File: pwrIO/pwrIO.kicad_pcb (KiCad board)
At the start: 4 copper layers, 33.7 x 30.3 mm, 55 parts, among them IC3 TLV61225DC, J1 MOTOR1, J2 MOTOR2, J3 VCC_MOTOR, J4 MOTOR1, J5 MOTOR2, J6 MISC, J7 ENC1, J8 ENC2, U1 TB6612FNG, U2 TB6612FNG

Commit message: sch pcb
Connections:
- R1 pad 1: /MOTOR_1/STBY -> /NB_B2
- R10 pad 1: /NB_B2 -> /MOTOR_2/PWMB
- R11 pad 1: /NB_B3 -> /NB_B5
- R12 pad 1: /NB_B4 -> /NB_A5
- R13 pad 1: /NB_B5 -> /NB_B6
- R14 pad 1: /NB_B6 -> /MOTOR_2/BIN2
- R2 pad 1: /NB_A1 -> /MOTOR_1/PWMA
- R3 pad 1: /NB_A2 -> /NB_A4
- R4 pad 1: /NB_A3 -> /NB_A2
- R5 pad 1: /NB_A4 -> /NB_B1
- R6 pad 1: /NB_A5 -> /NB_A3
- R7 pad 1: /NB_A6 -> /NB_B3
- R8 pad 1: /MOTOR_2/STBY -> /NB_A6
- R9 pad 1: /NB_B1 -> /NB_B4
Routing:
- net /NB_A4: track 7.34 -> 22.4 mm
- net /NB_A5: track 8.73 -> 23.4 mm
- net /NB_B6: track 0.00 -> 13.9 mm
- net /NB_A3: track 5.92 -> 19.2 mm
- net /NB_B2: track 0.00 -> 12.3 mm
- net /NB_B5: track 4.69 -> 15.9 mm
- net /NB_A6: track 10.5 -> 20.8 mm
- net /MOTOR_1/STBY: track 7.36 -> 0.00 mm
- net /NB_B4: track 11.8 -> 18.5 mm
- net /MOTOR_2/STBY: track 6.65 -> 0.00 mm
- net /NB_B3: track 9.80 -> 14.9 mm
- net /NB_A2: track 11.6 -> 16.3 mm
- net /NB_B1: track 13.0 -> 10.2 mm
- net /NB_A1: track 13.4 -> 14.9 mm

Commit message: sch pcb
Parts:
- C11, C5: moved to F.Cu
- moved C11 31.8 mm to (102.5, 70.4), turned to -90 degrees
- moved G*** 12.6 mm to (115.6, 83.7)
- moved C5 12.6 mm to (83.3, 70.3), turned to -90 degrees
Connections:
- R10 pad 1: /MOTOR_2/PWMB -> /NB_A8
- R14 pad 1: /MOTOR_2/BIN2 -> /NB_A7
- R2 pad 1: /MOTOR_1/PWMA -> /NB_A1
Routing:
- net /NB_A8: track 0.00 -> 19.8 mm
- net /NB_A7: track 0.00 -> 18.3 mm
- net /NB_B8: track 0.00 -> 10.9 mm
- net /NB_B7: track 0.00 -> 9.42 mm
- net GND1: track 34.9 -> 38.1 mm, vias 6 -> 9
- net GND: track 6.73 -> 8.53 mm, vias 4 -> 6

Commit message: pcb
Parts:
- moved G*** 11.7 mm to (104.1, 85.8)
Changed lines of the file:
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@@
 	(footprint "Cologne:open_cologne"
 		(layer "F.Cu")
-		(at 115.633146 83.705736)
+		(at 104.143146 85.825736)
 		(property "Reference" "G***"
 			(at 0 0 0)

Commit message: pcb
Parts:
- moved G*** 0.57 mm to (104.7, 85.9)
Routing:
- net VCC_MOTOR: track 30.9 -> 48.8 mm
- net +2V5: track 3.04 -> 10.2 mm
- net GND1: track 38.1 -> 44.7 mm
- net +3V3: track 20.9 -> 25.8 mm
- net GND: track 8.53 -> 11.3 mm, vias 6 -> 10

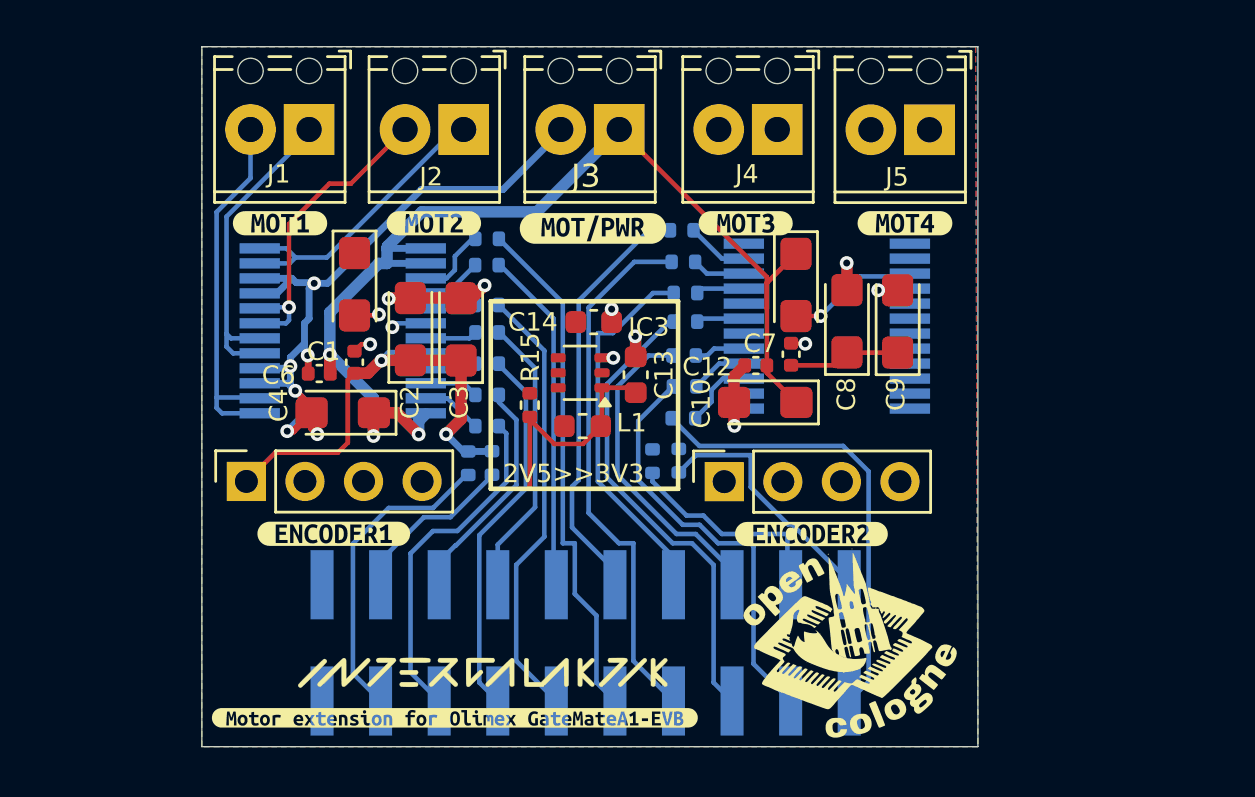
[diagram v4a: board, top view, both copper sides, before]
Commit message: Connecting encoder to 2.5V
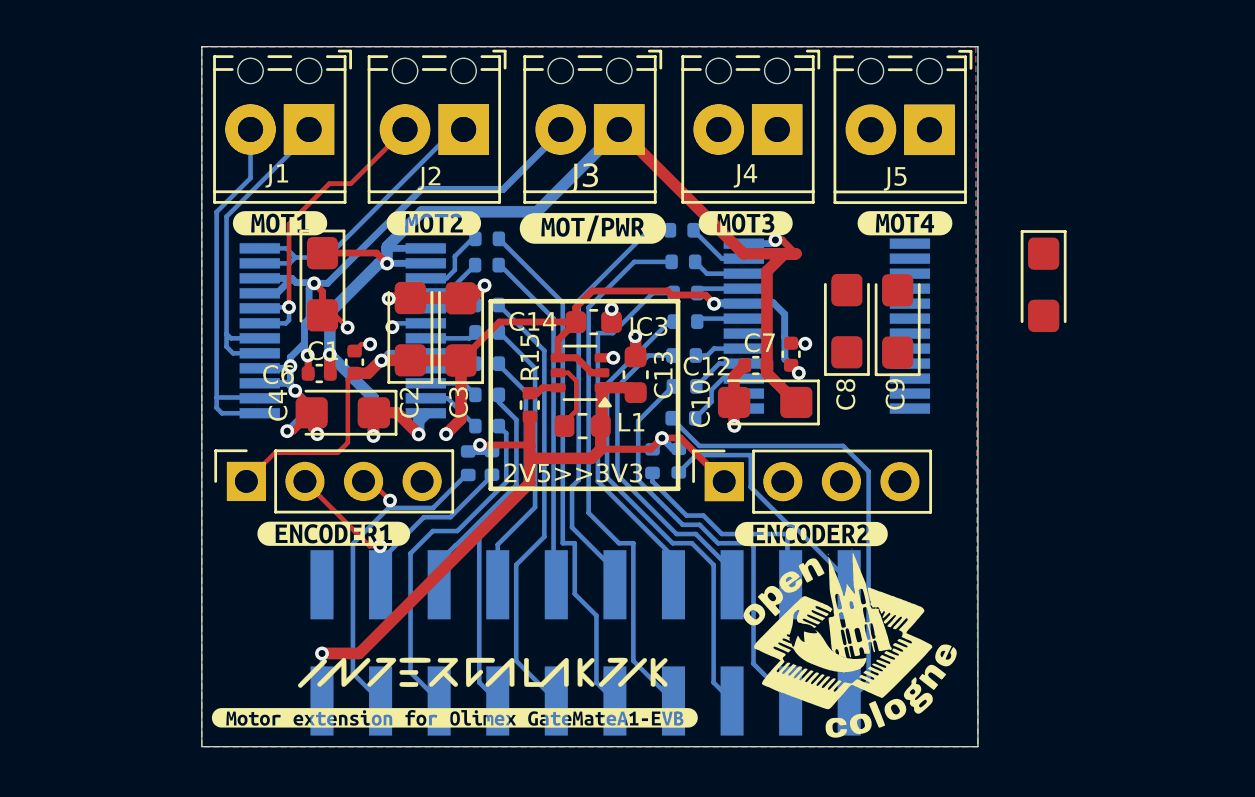
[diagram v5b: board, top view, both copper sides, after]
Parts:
- moved C11 10.7 mm to (113.2, 70.4)
- moved C5 1.39 mm to (81.9, 70.3)
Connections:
- J7 pad 1: +3V3 -> +2V5
- J8 pad 1: +3V3 -> +2V5
- R16 pad 1: +3V3 -> +2V5
- R17 pad 1: +3V3 -> +2V5
- R18 pad 1: +3V3 -> +2V5
- R19 pad 1: +3V3 -> +2V5
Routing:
- net +2V5: track 10.2 -> 36.1 mm, vias 0 -> 3
- net +3V3: track 25.8 -> 43.3 mm, vias 2 -> 4
- net /NB_B0: track 7.44 -> 13.5 mm, vias 0 -> 1
- net VCC_MOTOR: track 48.8 -> 54.2 mm, vias 3 -> 5
- net GND1: track 44.7 -> 40.6 mm, vias 9 -> 8
- net unconnected-(L1-Pad1): track 0.00 -> 3.10 mm
- net GND: track 11.3 -> 9.31 mm, vias 10 -> 8
- net /NB_A0: track 13.6 -> 15.4 mm, vias 0 -> 1
- net unconnected-(R15-Pad2): track 0.00 -> 1.33 mm

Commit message: initial connection done
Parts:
- removed G***: LOGO, PCM_Intergalaktik:Intergalaktik logo
- removed G***: LOGO, Cologne:open_cologne
- added H1: Logo Intergalaktik, intergalaktik:intergalaktik, F.Cu at (88.9, 87.3)
- added H2: Logo NLnet, nlnet:nlnet, F.Cu at (82.3, 84.2)
- added H3: Logo OpenCologne, Cologne:open_cologne, F.Cu at (104.0, 85.9)
- added H4: Logo Radiona, radiona:radiona, F.Cu at (92.2, 83.4)
- moved C11 8.82 mm to (105.2, 74.2), turned to 90 degrees
- moved C9 8.20 mm to (98.7, 72.2), turned to -90 degrees
- moved C10 7.00 mm to (104.3, 69.2), turned to 0 degrees
- moved C12 5.13 mm to (105.1, 71.2), turned to 0 degrees
- moved C8 3.81 mm to (100.9, 72.2), turned to -90 degrees
- moved kibuzzard-6746334D 1.81 mm to (104.9, 80.7)
- moved C7 1.68 mm to (102.5, 71.7), turned to -90 degrees
- moved J8 1.52 mm to (100.9, 78.7)
- moved kibuzzard-67464255 1.12 mm to (88.8, 89.4)
- moved R19 0.50 mm to (97.9, 78.0)
- moved kibuzzard-6746333A 0.48 mm to (82.4, 80.7)
- moved kibuzzard-674632F5 0.39 mm to (93.7, 67.5)
- moved kibuzzard-674632D6 0.39 mm to (106.9, 67.4)
- moved kibuzzard-674632A1 0.33 mm to (79.9, 67.4)
- moved kibuzzard-674632E9 0.30 mm to (100.3, 67.4)
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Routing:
- net GND1: track 40.6 -> 68.2 mm
- net Net-(J5-Pin_1): track 0.00 -> 16.2 mm, vias 0 -> 1
- net Net-(J4-Pin_1): track 0.00 -> 14.0 mm, vias 0 -> 1
- net Net-(J5-Pin_2): track 0.00 -> 14.0 mm, vias 0 -> 1
- net Net-(J4-Pin_2): track 0.00 -> 13.5 mm, vias 0 -> 1
- net +2V5: track 36.1 -> 48.4 mm, vias 3 -> 4
- net +3V3: track 43.3 -> 31.6 mm, vias 4 -> 2
- net VCC_MOTOR: track 54.2 -> 63.5 mm, vias 5 -> 6
- net /NB_B7: track 9.42 -> 13.7 mm, vias 0 -> 1
- net GND: track 9.31 -> 11.7 mm, vias 8 -> 32
- net /NB_B8: track 10.9 -> 13.2 mm
- net /NB_A8: track 19.8 -> 17.6 mm
- net Net-(U2-PWMB): track 3.13 -> 2.22 mm
- net /NB_B6: track 14.1 -> 13.5 mm
- net Net-(J2-Pin_2): track 13.5 -> 13.0 mm
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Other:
- board size 33.7 x 30.3 mm -> 33.7 x 30.5 mm

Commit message: Updating pdf - adding blender export
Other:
- board text added: "PCB3D_BR_pwrIO"
- board text added: "PCB3D_TL_pwrIO"
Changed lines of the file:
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@@
 		)
+	)
+	(gr_text "PCB3D_BR_pwrIO"
+		(at 110.36 90.53 180)
+		(layer "Cmts.User")
+		(effects
+			(font
+				(size 1 1)
+				(thickness 0.2)
+				(bold yes)
+			)
+			(justify left bottom)
+		)
+	)
+	(gr_text "PCB3D_TL_pwrIO"
+		(at 76.71 60.03 0)
+		(layer "Cmts.User")
+		(effects
+			(font
+				(size 1 1)
+				(thickness 0.2)
+				(bold yes)
+			)
+			(justify left bottom)
+		)
+	)
+	(dimension
+		(type aligned)
+		(layer "Dwgs.User")
+		(pts
+			(xy 76.71 60.03) (xy 110.36 60.03)
+		)
+		(height -3.4)
+		(gr_text "33.6500 mm"
+			(at 93.535 55.48 0)
+			(layer "Dwgs.User")
+			(effects
+				(font
+					(size 1 1)
+					(thickness 0.15)
+				)
+			)
+		)
+		(format
+			(prefix "")
+			(suffix "")
+			(units 3)
+			(units_format 1)
+			(precision 4)
+		)
+		(style
+			(thickness 0.1)
+			(arrow_length 1.27)
+			(text_position_mode 0)
+			(extension_height 0.58642)
+			(extension_offset 0.5) keep_text_aligned)
+	)
+	(dimension
+		(type aligned)
+		(layer "Dwgs.User")
+		(pts
+			(xy 76.71 60.03) (xy 76.71 90.53)
+		)
+		(height 2.889999)
+		(gr_text "30.5000 mm"
+			(at 72.670001 75.28 90)
+			(layer "Dwgs.User")
+			(effects
+				(font
+					(size 1 1)
+					(thickness 0.15)
+				)
+			)
+		)
+		(format
+			(prefix "")
+			(suffix "")
+			(units 3)
+			(units_format 1)
+			(precision 4)
+		)
+		(style
+			(thickness 0.1)
+			(arrow_length 1.27)
+			(text_position_mode 0)
+			(extension_height 0.58642)
+			(extension_offset 0.5) keep_text_aligned)
 	)
 	(segment

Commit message: PCB update
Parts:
- moved H3 0.26 mm to (104.0, 85.7)
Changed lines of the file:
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@@
 		)
 		(property "Value" "100n"
-			(at 0 1.16 270)
+			(at 0 1.16 -90)
 			(layer "F.Fab")
 			(effects
@@
 		)
 		(fp_text user "${REFERENCE}"
-			(at 0 0 270)
+			(at 0 0 -90)
 			(layer "F.Fab")
 			(effects
@@
 		(tags "capacitor tantalum")
 		(property "Reference" "C8"
-			(at 3.072501 0.05 270)
+			(at 3.072501 0.05 -90)
 			(layer "F.SilkS")
 			(effects
@@
 		)
 		(property "Value" "10u"
-			(at 0 1.75 270)
+			(at 0 1.75 -90)
 			(layer "F.Fab")
 			(effects
@@
 		)
 		(fp_text user "${REFERENCE}"
-			(at 0 0 270)
+			(at 0 0 -90)
 			(layer "F.Fab")
 			(effects
@@
 	(footprint "Cologne:open_cologne"
 		(layer "F.Cu")
-		(at 104.02 85.94)
+		(at 104.02 85.675736)
 		(property "Reference" "H3"
 			(at 0 0 0)
@@
 		(tags "capacitor tantalum")
 		(property "Reference" "C9"
-			(at 3.082501 -0.02 270)
+			(at 3.082501 -0.02 -90)
 			(layer "F.SilkS")
 			(effects
@@
 		)
 		(property "Value" "10u"
-			(at 0 1.75 270)
+			(at 0 1.75 -90)
 			(layer "F.Fab")
 			(effects
@@
 		)
 		(fp_text user "${REFERENCE}"
-			(at 0 0 270)
+			(at 0 0 -90)
 			(layer "F.Fab")
 			(effects
@@
 		(tags "THT Terminal Block Phoenix MPT-0,5-2-2.54 pitch 2.54mm size 5.54x6.2mm^2 drill 1.1mm pad 2.2mm")
 		(property "Reference" "J4"
-			(at 1.319999 -1.93 360)
+			(at 1.319999 -1.93 0)
 			(layer "F.SilkS")
 			(effects
@@
 		)
 		(fp_text user "${REFERENCE}"
-			(at 1.27 1.999999 360)
+			(at 1.27 1.999999 0)
 			(layer "F.Fab")
 			(effects
@@
 		(tags "THT Terminal Block Phoenix MPT-0,5-2-2.54 pitch 2.54mm size 5.54x6.2mm^2 drill 1.1mm pad 2.2mm")
 		(property "Reference" "J5"
-			(at 1.409999 -2.05 360)
+			(at 1.409999 -2.05 0)
 			(layer "F.SilkS")
 			(effects
@@
 		)
 		(fp_text user "${REFERENCE}"
-			(at 1.27 1.999999 360)
+			(at 1.27 1.999999 0)
 			(layer "F.Fab")
 			(effects
@@
 		)
 		(property "Value" "10u"
-			(at 48.84 -12.709999 270)
+			(at 48.84 -12.709999 -90)
 			(layer "F.Fab")
 			(effects
@@
 		)
 		(fp_text user "${REFERENCE}"
-			(at -1.43 1.529999 270)
+			(at -1.43 1.529999 -90)
 			(layer "F.Fab")
 			(effects
